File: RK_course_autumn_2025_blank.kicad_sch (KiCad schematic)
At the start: 24 parts, among them J1 JST-ZH 6pin, J2 JST-ZH 6pin, J3 Conn_01x02, J4 JST-ZH 6pin, J5 JST-ZH 6pin, J6 Conn_01x03

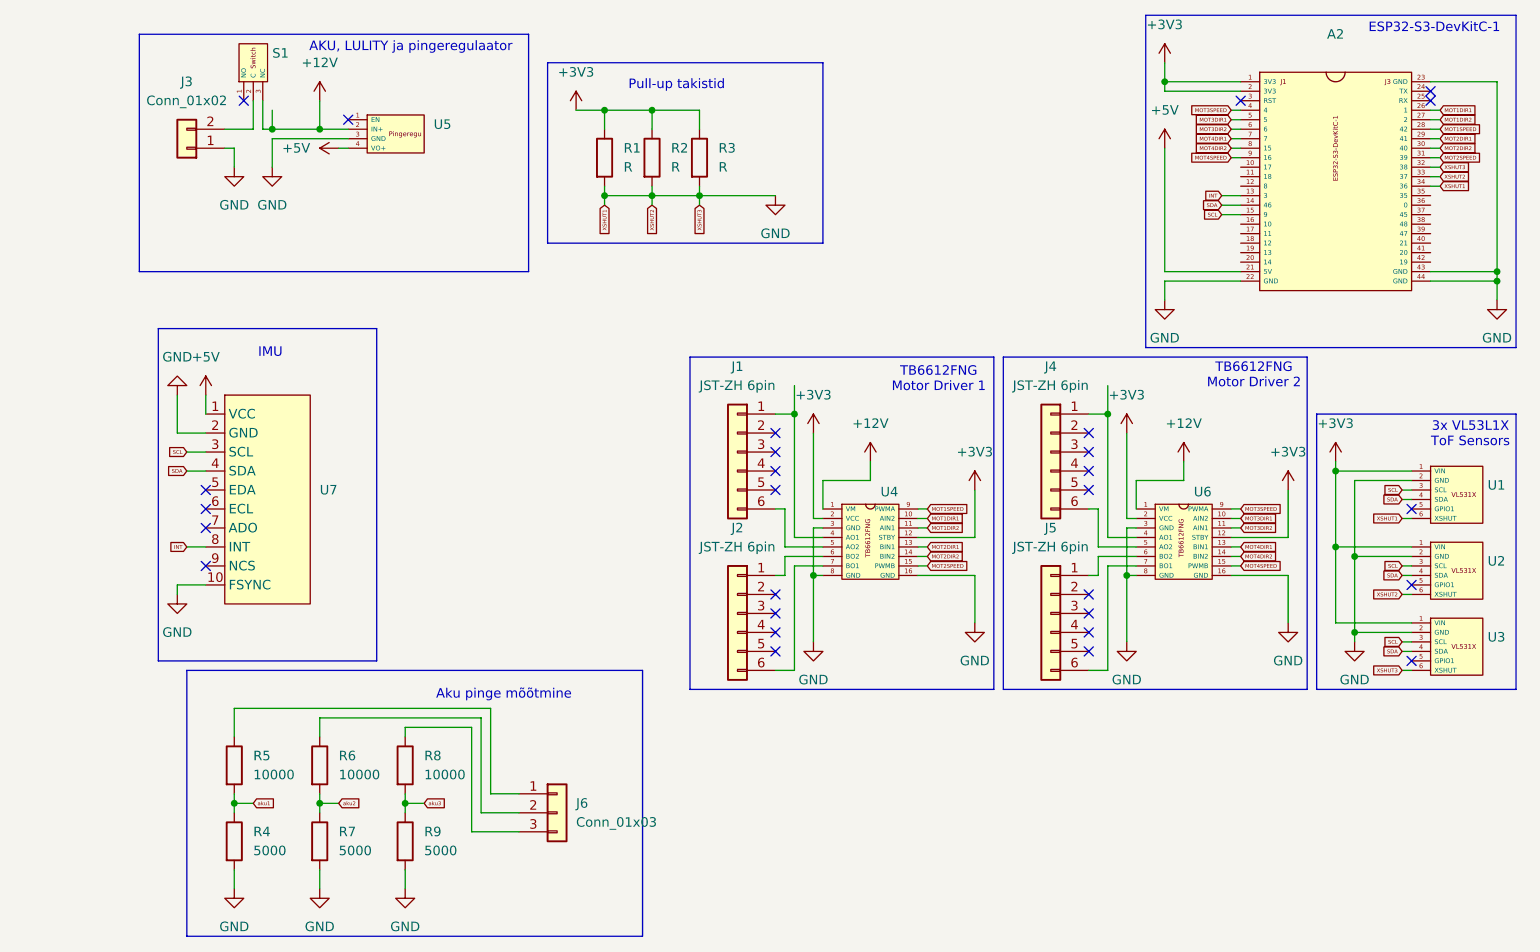
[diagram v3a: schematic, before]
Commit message: Fixed pull-up resistors, added battery voltage measurement, better pin connection layout
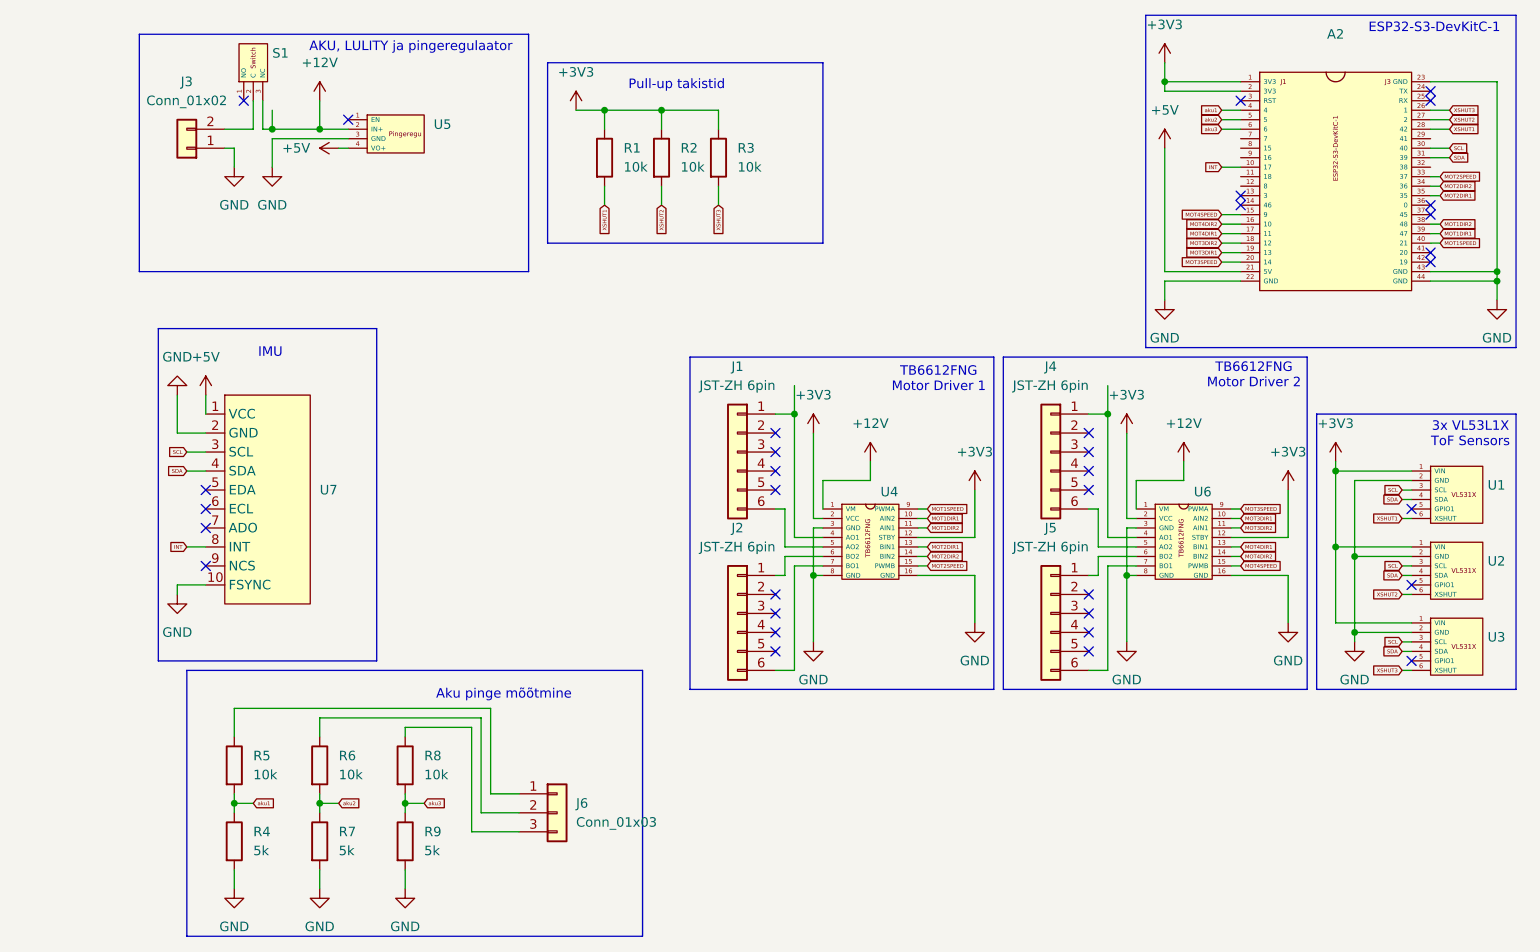
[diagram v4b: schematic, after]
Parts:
- R1, R2, R3: value R -> 10k
- R4, R7, R9: value 5000 -> 5k
- R5, R6, R8: value 10000 -> 10k
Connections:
- net GND: no longer A2.32 (38), A2.33 (37), A2.34 (36), R1.2, R2.2, R3.2, U1.6 (XSHUT), U2.6 (XSHUT), U3.6 (XSHUT)
- net INT: now also A2.10 (17); no longer A2.13 (3)
- net MOT1DIR1: now also A2.39 (47); no longer A2.26 (1)
- net MOT1DIR2: now also A2.38 (48); no longer A2.27 (2)
- net MOT1SPEED: now also A2.40 (21); no longer A2.28 (42)
- net MOT2DIR1: now also A2.35; no longer A2.29 (41)
- net MOT2DIR2: now also A2.34 (36); no longer A2.30 (40)
- net MOT2SPEED: now also A2.33 (37); no longer A2.31 (39)
- net MOT3DIR1: now also A2.19 (13); no longer A2.5
- net MOT3DIR2: now also A2.18 (12); no longer A2.6
- net MOT3SPEED: now also A2.20 (14); no longer A2.4
- net MOT4DIR1: now also A2.17 (11); no longer A2.7
- net MOT4DIR2: now also A2.16 (10); no longer A2.8 (15)
- net MOT4SPEED: now also A2.15 (9); no longer A2.9 (16)
- net SCL: now also A2.30 (40); no longer A2.15 (9)
- net SDA: now also A2.31 (39); no longer A2.14 (46)
- net aku1: now also A2.4
- net aku2: now also A2.5
- net aku3: now also A2.6
- new net XSHUT1: A2.28 (42), R1.2, U1.6 (XSHUT)
- new net XSHUT2: A2.27 (2), R2.2, U2.6 (XSHUT)
- new net XSHUT3: A2.26 (1), R3.2, U3.6 (XSHUT)
- no-connect marks 28 -> 34
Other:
- moved on the sheet: R2, R3

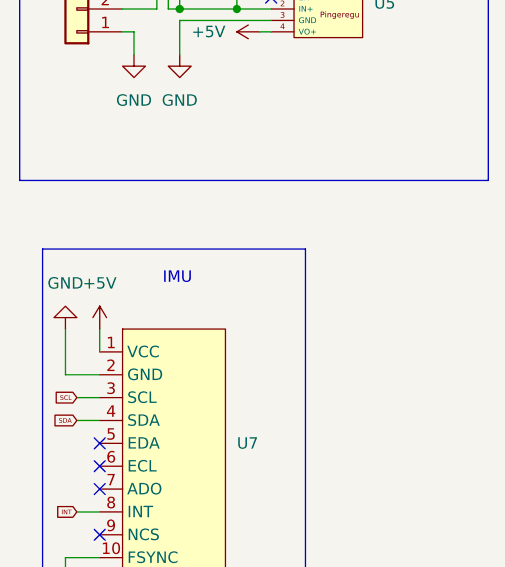
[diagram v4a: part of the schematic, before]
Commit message: Added traces to PCB to see if possible. Has to be done again.
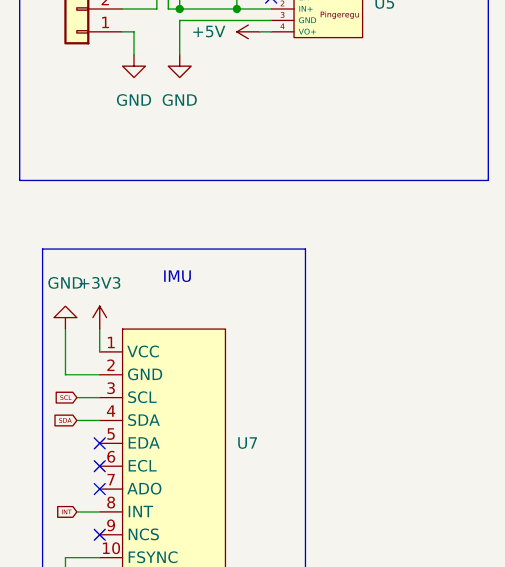
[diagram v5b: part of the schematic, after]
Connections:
- net +3V3: now also U7.1 (VCC)
- net +5V: no longer U7.1 (VCC)
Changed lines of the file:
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@@
+	)
+	(symbol
+		(lib_id "power:+3V3")
+		(at 21.59 63.5 0)
+		(unit 1)
+		(exclude_from_sim no)
+		(in_bom yes)
+		(on_board yes)
+		(dnp no)
+		(fields_autoplaced yes)
+		(property "Reference" "#PWR022"
+			(at 21.59 67.31 0)
+			(effects
+				(font
+					(size 1.27 1.27)
+				)
+				(hide yes)
+			)
+		)
+		(property "Value" "+3V3"
+			(at 21.59 58.42 0)
+			(effects
+				(font
+					(size 1.27 1.27)
+				)
+			)
+		)
+		(property "Footprint" ""
+			(at 21.59 63.5 0)
+			(effects
+				(font
+					(size 1.27 1.27)
+				)
+				(hide yes)
+			)
+		)
+		(property "Datasheet" ""
+			(at 21.59 63.5 0)
+			(effects
+				(font
+					(size 1.27 1.27)
+				)
+				(hide yes)
+			)
+		)
+		(property "Description" "Power symbol creates a global label with name \"+3V3\""
+			(at 21.59 63.5 0)
+			(effects
+				(font
+					(size 1.27 1.27)
+				)
+				(hide yes)
+			)
+		)
+		(pin "1"
+		)
+		(instances
+			(project ""
+				(path "/a85e8d7d-6e69-4ae0-af3b-65bd111e6aa4"
+					(reference "#PWR022")
+					(unit 1)
+				)
+			)
+		)
 	)
 	(symbol
@@
 					(unit 1)
 				)
-			)
-		)
-	)
-	(symbol
-		(lib_id "power:+5V")
-		(at 21.59 63.5 0)
-		(unit 1)
-		(exclude_from_sim no)
-		(in_bom yes)
-		(on_board yes)
-		(dnp no)
-		(fields_autoplaced yes)
-		(property "Reference" "#PWR022"
-			(at 21.59 67.31 0)
-			(effects
-				(font
-					(size 1.27 1.27)
-				)
-				(hide yes)
-			)
-		)
-		(property "Value" "+5V"
-			(at 21.59 58.42 0)
-			(effects
-				(font
-					(size 1.27 1.27)
-				)
-			)
-		)
-		(property "Footprint" ""
-			(at 21.59 63.5 0)
-			(effects
-				(font
-					(size 1.27 1.27)
-				)
-				(hide yes)
-			)
-		)
-		(property "Datasheet" ""
-			(at 21.59 63.5 0)
-			(effects
-				(font
-					(size 1.27 1.27)
-				)
-				(hide yes)
-			)
-		)
-		(property "Description" "Power symbol creates a global label with name \"+5V\""
-			(at 21.59 63.5 0)
-			(effects
-				(font
-					(size 1.27 1.27)
-				)
-				(hide yes)
-			)
-		)
-		(pin "1"
-		)
-		(instances
-			(project ""
-				(path "/a85e8d7d-6e69-4ae0-af3b-65bd111e6aa4"
-					(reference "#PWR022")
-					(unit 1)
-				)

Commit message: added connector for oled monitor, fixed i2c pins
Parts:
- removed J6: Conn_01x03, Connector_PinHeader_2.54mm:PinHeader_1x03_P2.54mm_Vertical, symbol Connector_Generic:Conn_01x03
- removed R6, R8: 10k, Resistor_SMD:R_0603_1608Metric_Pad0.98x0.95mm_HandSolder, symbol Device:R
- removed R7, R9: 5k, Resistor_SMD:R_0603_1608Metric_Pad0.98x0.95mm_HandSolder, symbol Device:R
- added J6: Conn_01x04, Connector_PinHeader_2.54mm:PinHeader_1x04_P2.54mm_Vertical, symbol Connector_Generic:Conn_01x04
- R5: value 10k -> 15k
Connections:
- net +12V: now also R5.1
- net +3V3: now also J6.2 (Pin_2)
- net GND: now also J6.1 (Pin_1)
- net MOT4SPEED: now also A2.11 (18); no longer A2.15 (9)
- net SCL: now also A2.15 (9), J6.3 (Pin_3); no longer A2.30 (40)
- net SDA: now also A2.12 (8), J6.4 (Pin_4); no longer A2.31 (39)
- net aku2: no longer names the net of A2.5
- net aku3: no longer names the net of A2.6
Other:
- note added: "OLED monitor"

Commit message: new schematic, PCB tracks not final
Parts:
- added JP1: SolderJumper_3_Open, Jumper:SolderJumper-3_P1.3mm_Open_RoundedPad1.0x1.5mm, symbol Jumper:SolderJumper_3_Open
- added JP2, JP3, JP4, JP5: SolderJumper_2_Open, Jumper:SolderJumper-2_P1.3mm_Open_RoundedPad1.0x1.5mm, symbol Jumper:SolderJumper_2_Open
- added R8: 15k, Resistor_SMD:R_0603_1608Metric_Pad0.98x0.95mm_HandSolder, symbol Device:R
- added R9: 4k7, Resistor_SMD:R_0603_1608Metric_Pad0.98x0.95mm_HandSolder, symbol Device:R
- R4: value 5k -> 4k7
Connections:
- net +12V: now also R8.1
- net +3V3: now also J1.5 (Pin_5), J2.5 (Pin_5), J4.5 (Pin_5), J5.5 (Pin_5), JP1.3 (B); no longer U4.12 (STBY), U6.12 (STBY)
- net GND: now also J1.2 (Pin_2), J2.2 (Pin_2), J4.2 (Pin_2), J5.2 (Pin_2), JP1.1 (A), R9.2
- net INT: now also A2.5; no longer A2.10 (17)
- net MOT2DIR1: now also A2.32 (38); no longer A2.35
- net MOT2DIR2: now also A2.30 (40); no longer A2.34 (36)
- net MOT2SPEED: now also A2.29 (41); no longer A2.33 (37)
- net MOT3ENC0: now reaches J4.3 (Pin_3)
- net MOT3ENC0: now also A2.10 (17)
- net MOT3ENC1: now reaches J4.4 (Pin_4)
- net MOT3ENC1: now also A2.9 (16)
- net MOT1ENC0: now reaches J1.3 (Pin_3)
- net MOT1ENC0: now also JP4.2 (B)
- net MOT1ENC1: now reaches J1.4 (Pin_4)
- net MOT1ENC1: now also JP5.2 (B)
- net MOT4ENC0: now reaches J5.3 (Pin_3)
- net MOT4ENC0: now also A2.8 (15)
- net MOT4ENC1: now reaches J5.4 (Pin_4)
- net MOT4ENC1: now also A2.7
- net at A2.31 (39): now also JP2.1 (A)
- net MOT2ENC0: now reaches J2.3 (Pin_3)
- net MOT2ENC0: now also JP2.2 (B)
- net MOT2ENC1: now reaches J2.4 (Pin_4)
- net MOT2ENC1: now also JP3.2 (B)
- net at U7.7 (ADO): now also JP1.2 (C)
- new net: A2.33 (37), JP3.1 (A)
- new net: A2.34 (36), JP4.1 (A)
- new net: A2.35, JP5.1 (A)
- new net STBY: R8.2, R9.1, U4.12 (STBY), U6.12 (STBY)
- no-connect marks 34 -> 17
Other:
- note added: "Standby mootori draverid"
- moved on the sheet: A2, U7

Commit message: now with tracks
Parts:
- added R6: 15k, Resistor_SMD:R_0603_1608Metric_Pad0.98x0.95mm_HandSolder, symbol Device:R
- added R7: 4k7, Resistor_SMD:R_0603_1608Metric_Pad0.98x0.95mm_HandSolder, symbol Device:R
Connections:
- net +12V: now also R6.1
- net GND: now also R7.2
- net MOT1ENC0: now also JP5.2 (B); no longer JP4.2 (B)
- net MOT1ENC1: now also JP4.2 (B); no longer JP5.2 (B)
- net MOT3ENC0: now also A2.8 (15); no longer A2.10 (17)
- net MOT3ENC1: now also A2.7; no longer A2.9 (16)
- net MOT4ENC0: now also A2.10 (17); no longer A2.8 (15)
- net MOT4ENC1: now also A2.9 (16); no longer A2.7
- net STBY renamed STBY1
- net STBY1: no longer U6.12 (STBY)
- new net STBY2: R6.2, R7.1, U6.12 (STBY)
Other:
- note added: "Standby mootori draver 1"
- note added: "Standby mootori draver 2"
- note removed: "Standby mootori draverid"
